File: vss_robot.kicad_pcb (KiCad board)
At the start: 2 copper layers, 65 x 65 mm, 14 parts, among them J2 Conn_01x04_Socket, J3 Conn_01x02_Socket, J4 Conn_01x02_Socket, J5 Conn_01x06_Socket, SW1 SW_Push, U1 LM1117DT-3.3, U2 NRF24L01_Breakout, U4 ESP32-DEVKIT-V1

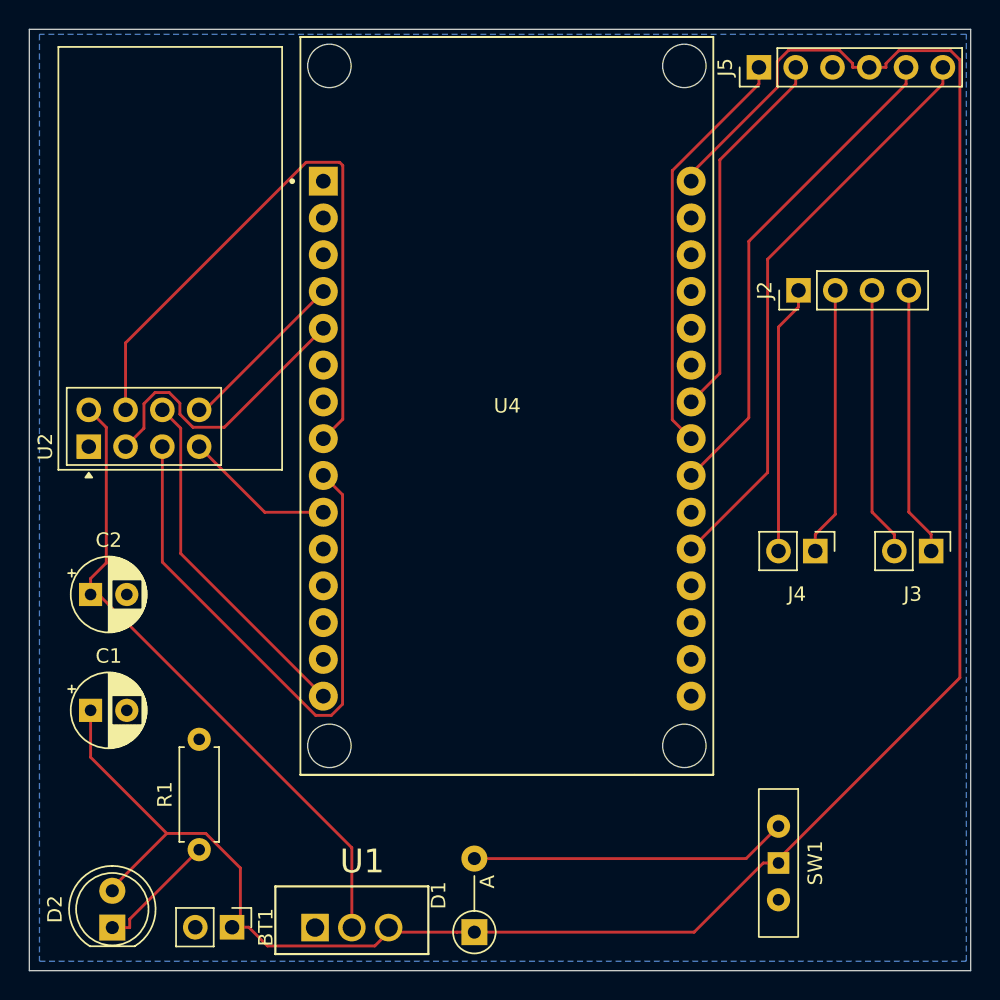
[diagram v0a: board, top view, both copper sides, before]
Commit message: grossura da trilha, layer e posicionamento
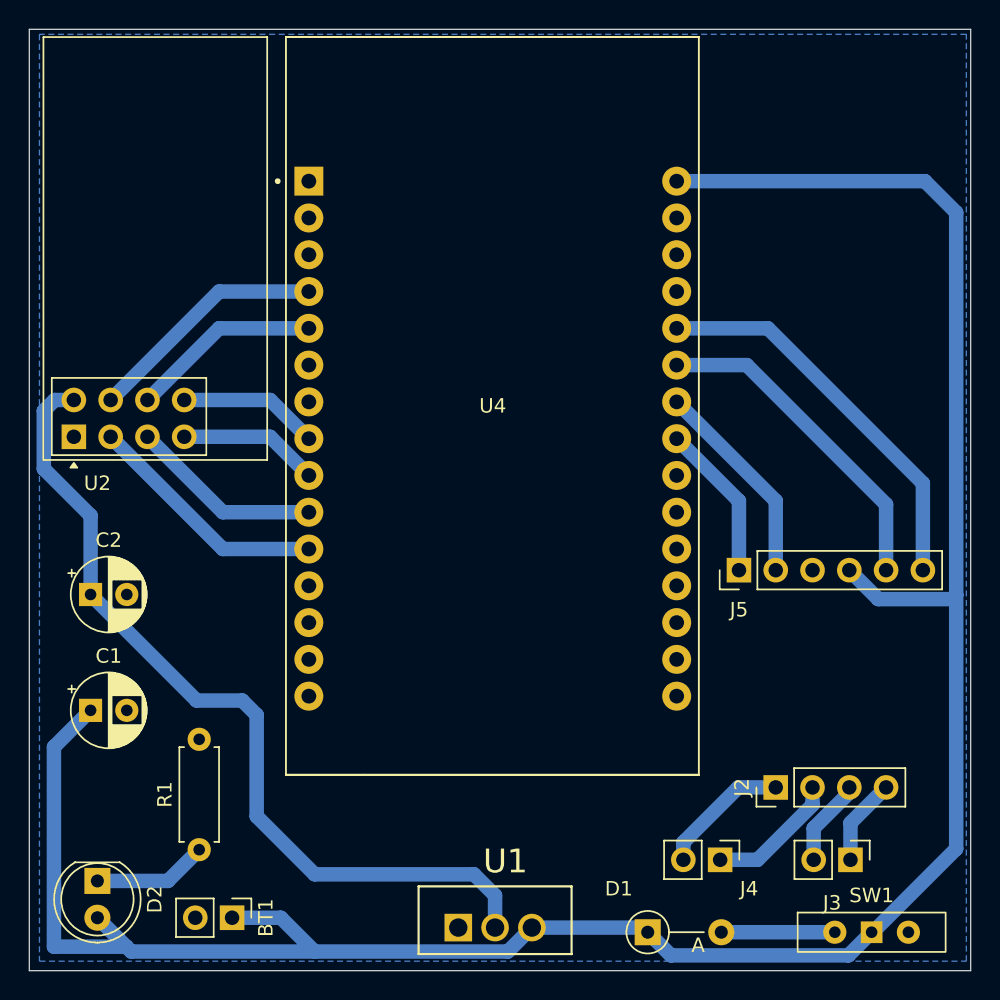
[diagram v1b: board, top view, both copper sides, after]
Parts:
- moved J5 34.7 mm to (166.3, 96.0)
- moved J2 34.4 mm to (168.8, 111.0)
- moved J4 22.3 mm to (165.0, 116.0)
- moved J3 22.0 mm to (174.0, 116.0)
- moved D1 12.0 mm to (160.0, 121.0), turned to 0 degrees
- moved U1 9.89 mm to (152.0, 119.7)
- moved SW1 8.01 mm to (175.5, 121.0), turned to 0 degrees
- moved D2 3.38 mm to (122.0, 117.5), turned to -90 degrees
- moved U2 1.23 mm to (120.4, 86.8)
- moved U4 1.00 mm to (149.3, 84.7)
- moved BT1 0.66 mm to (131.3, 120.0)
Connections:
- U4 pad 10: /MISO -> /SCK
- U4 pad 11: unconnected-(U4-D21-Pad11) -> /CE
- U4 pad 15: /MOSI -> unconnected-(U4-D23-Pad15)
- U4 pad 20: Net-(J5-Pin_6) -> unconnected-(U4-D35-Pad20)
- U4 pad 22: Net-(J5-Pin_5) -> unconnected-(U4-D33-Pad22)
- U4 pad 25: unconnected-(U4-D27-Pad25) -> Net-(J5-Pin_5)
- U4 pad 26: unconnected-(U4-D14-Pad26) -> Net-(J5-Pin_6)
- U4 pad 4: /IRQ -> /CSN
- U4 pad 5: /CE -> /MOSI
- U4 pad 8: /CSN -> /IRQ
- U4 pad 9: /SCK -> /MISO
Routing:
- net /SCK: track 41.5 -> 13.3 mm
- net /CSN: track 44.3 -> 16.8 mm
- net Net-(J5-Pin_1): track 28.7 -> 10.9 mm
- net 3V3: track 44.7 -> 59.3 mm
- net Net-(D1-A): track 21.9 -> 7.84 mm
- net VCC: track 153.3 -> 166.7 mm
- net Net-(J5-Pin_6): track 40.5 -> 27.4 mm
- net Net-(J2-Pin_4): track 18.6 -> 6.02 mm
- net Net-(J2-Pin_3): track 18.6 -> 6.02 mm
- net Net-(J5-Pin_2): track 26.1 -> 14.5 mm
- net /MOSI: track 24.4 -> 13.2 mm
- net Net-(J5-Pin_5): track 34.3 -> 23.3 mm
- net Net-(J2-Pin_2): track 18.6 -> 9.15 mm
- net Net-(J2-Pin_1): track 18.6 -> 9.15 mm
- net /CE: track 20.5 -> 16.9 mm
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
